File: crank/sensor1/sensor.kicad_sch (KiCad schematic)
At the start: 12 parts, among them J1 Conn_01x03_Socket, J2 Conn_01x04_Pin, Q1 2N3904, U1 TLV493D, U2 SeeeduinoXIAO

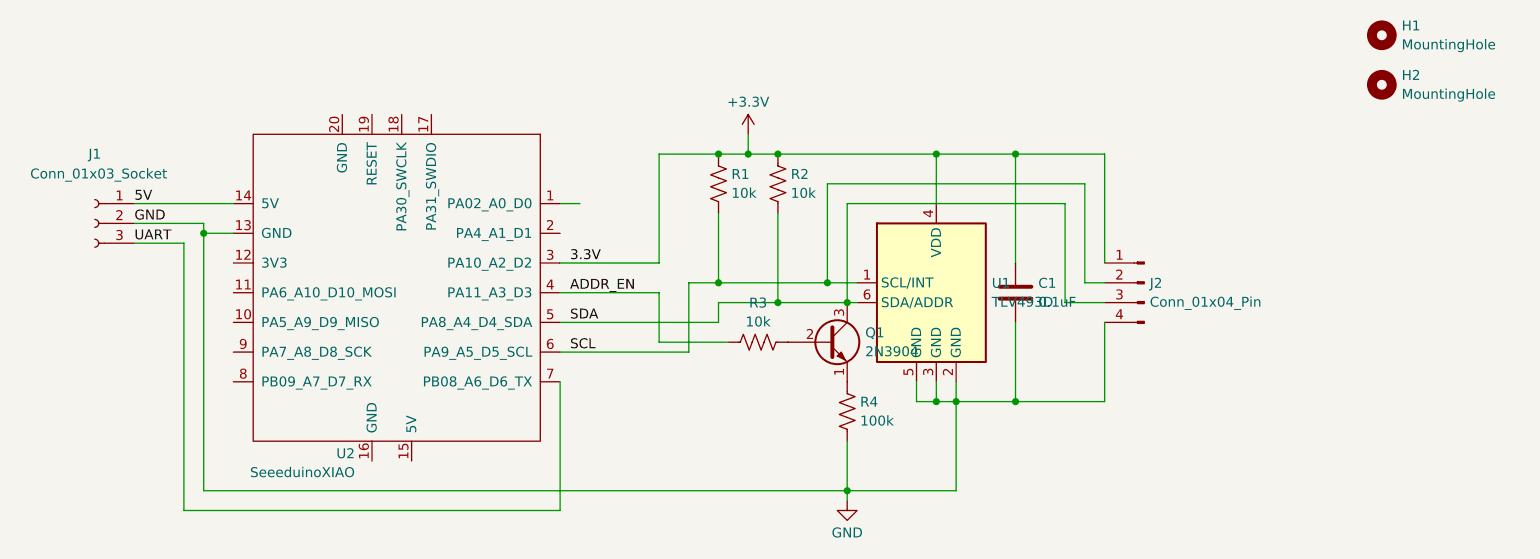
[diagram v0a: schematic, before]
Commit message: removed dumb switch, forgot that I could just power the second sensor directly from gpio
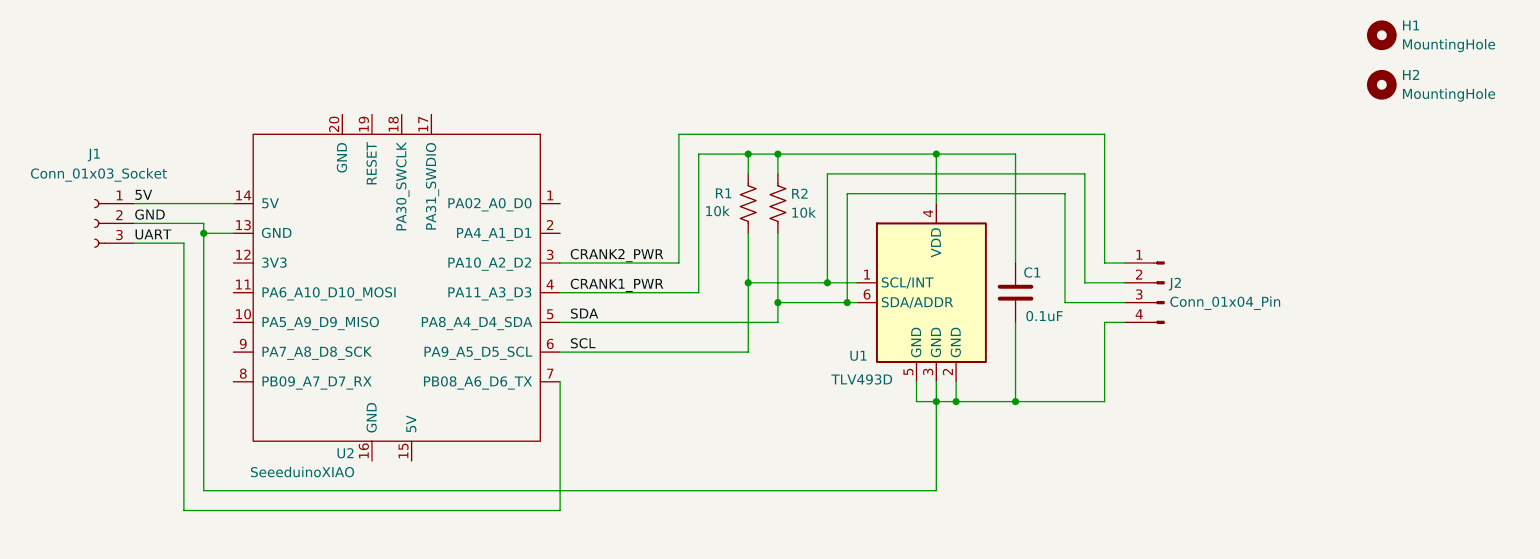
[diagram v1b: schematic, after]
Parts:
- removed Q1: 2N3904, Package_TO_SOT_SMD:SOT-23, symbol Transistor_BJT:2N3904
- removed R3: 10k, Resistor_SMD:R_0603_1608Metric, symbol Device:R_US
- removed R4: 100k, Resistor_SMD:R_0603_1608Metric, symbol Device:R_US
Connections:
- net ADDR_EN is gone; now on net CRANK1_PWR: U2.4 (PA11_A3_D3)
- net +3.3V renamed CRANK1_PWR
- net CRANK1_PWR: no longer J2.1 (Pin_1), U2.3 (PA10_A2_D2)
- new net CRANK2_PWR: J2.1 (Pin_1), U2.3 (PA10_A2_D2)
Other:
- moved on the sheet: J2, R1, R2
